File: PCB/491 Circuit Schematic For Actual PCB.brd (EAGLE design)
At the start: 160 x 100 mm, 27 parts

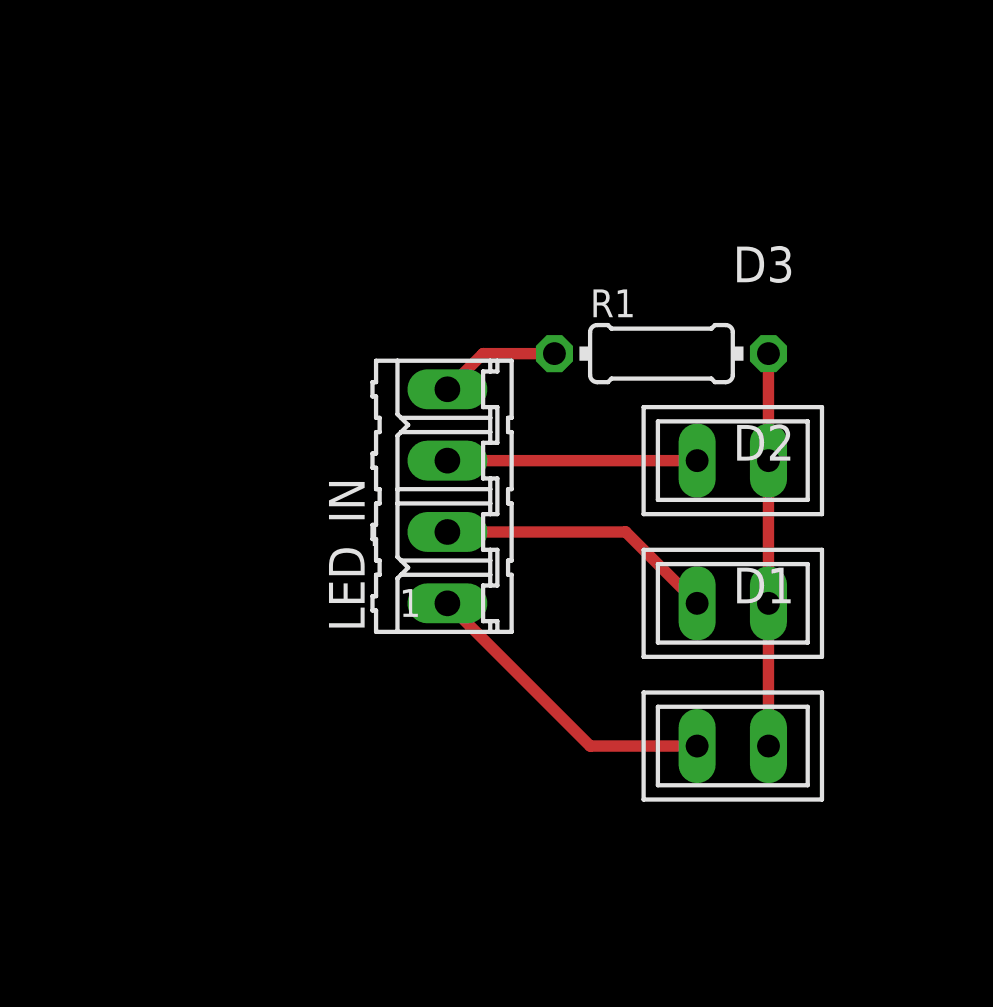
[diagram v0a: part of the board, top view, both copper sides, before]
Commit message: Added 5mm LEDs
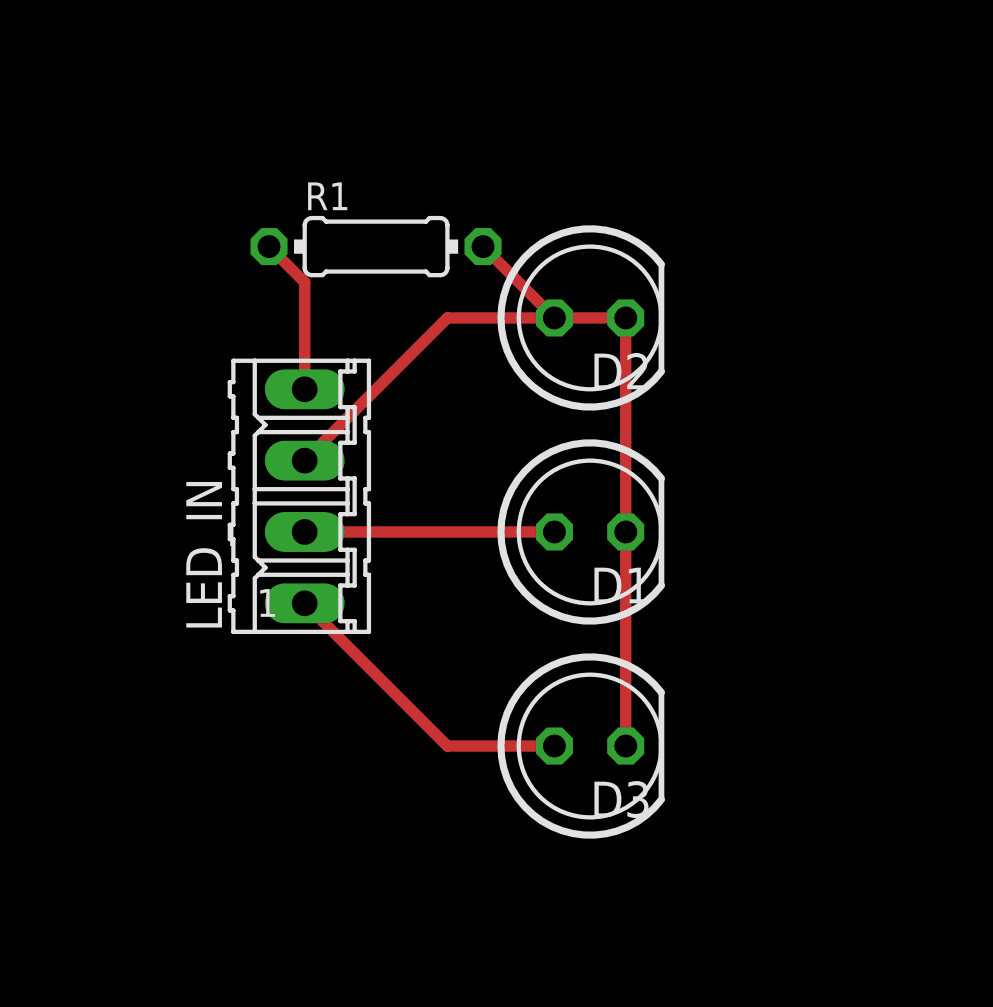
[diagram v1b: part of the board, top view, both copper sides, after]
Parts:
- D1, D2, D3: value U57X32 -> (none); device led:U57X32 -> led:LED5MM
- moved R1 10.9 mm to (135.9, 59.7)
- moved D3 7.18 mm to (143.5, 57.1)
- moved D2 5.68 mm to (143.5, 49.5)
- moved D1 5.08 mm to (143.5, 41.9)
- moved LED_IN 5.08 mm to (133.3, 50.8)
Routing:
- net N$10: track 14.0 -> 21.4 mm
- net N$1: track 8.89 -> 11.0 mm
- net N$30: track 4.34 -> 5.61 mm
- net N$3: track 9.94 -> 8.89 mm
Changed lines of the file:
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@@
 </autorouter>
 <elements>
-<element name="D1" library="led" library_urn="urn:adsk.eagle:library:259" package="U57X32" package3d_urn="urn:adsk.eagle:package:15789/1" value="U57X32" x="148.59" y="41.91" smashed="yes">
-<attribute name="NAME" x="148.59" y="46.99" size="1.27" layer="25" ratio="10"/>
-<attribute name="POPULARITY" value="0" x="148.59" y="41.91" size="1.778" layer="27" display="off"/>
-<attribute name="VALUE" x="148.59" y="44.45" size="1.27" layer="27" ratio="10"/>
-</element>
-<element name="D2" library="led" library_urn="urn:adsk.eagle:library:259" package="U57X32" package3d_urn="urn:adsk.eagle:package:15789/1" value="U57X32" x="148.59" y="46.99" smashed="yes">
-<attribute name="NAME" x="148.59" y="52.07" size="1.27" layer="25" ratio="10"/>
-<attribute name="POPULARITY" value="0" x="148.59" y="46.99" size="1.778" layer="27" display="off"/>
-<attribute name="VALUE" x="148.59" y="49.53" size="1.27" layer="27" ratio="10"/>
-</element>
-<element name="D3" library="led" library_urn="urn:adsk.eagle:library:259" package="U57X32" package3d_urn="urn:adsk.eagle:package:15789/1" value="U57X32" x="148.59" y="52.07" smashed="yes">
-<attribute name="NAME" x="148.59" y="58.42" size="1.27" layer="25" ratio="10"/>
-<attribute name="POPULARITY" value="0" x="148.59" y="52.07" size="1.778" layer="27" display="off"/>
-<attribute name="VALUE" x="148.59" y="55.88" size="1.27" layer="27" ratio="10"/>
+<element name="D1" library="led" library_urn="urn:adsk.eagle:library:259" package="LED5MM" package3d_urn="urn:adsk.eagle:package:15799/2" value="" x="143.51" y="41.91" smashed="yes">
+<attribute name="NAME" x="143.51" y="46.99" size="1.27" layer="25" ratio="10"/>
+<attribute name="POPULARITY" value="93" x="143.51" y="41.91" size="1.778" layer="27" display="off"/>
+<attribute name="VALUE" x="143.51" y="44.45" size="1.27" layer="27" ratio="10"/>
+</element>
+<element name="D2" library="led" library_urn="urn:adsk.eagle:library:259" package="LED5MM" package3d_urn="urn:adsk.eagle:package:15799/2" value="" x="143.51" y="49.53" smashed="yes">
+<attribute name="NAME" x="143.51" y="54.61" size="1.27" layer="25" ratio="10"/>
+<attribute name="POPULARITY" value="93" x="143.51" y="49.53" size="1.778" layer="27" display="off"/>
+<attribute name="VALUE" x="143.51" y="52.07" size="1.27" layer="27" ratio="10"/>
+</element>
+<element name="D3" library="led" library_urn="urn:adsk.eagle:library:259" package="LED5MM" package3d_urn="urn:adsk.eagle:package:15799/2" value="" x="143.51" y="57.15" smashed="yes">
+<attribute name="NAME" x="143.51" y="39.37" size="1.27" layer="25" ratio="10"/>
+<attribute name="POPULARITY" value="93" x="143.51" y="57.15" size="1.778" layer="27" display="off"/>
+<attribute name="VALUE" x="143.51" y="60.96" size="1.27" layer="27" ratio="10"/>
 </element>
 <element name="RELAY" library="SRD-05VDC-SL-C" package="RELAY_SRD-05VDC-SL-C" value="SRD-05VDC-SL-C" x="34.29" y="25.4" smashed="yes" rot="R270">
@@
 <element name="U$1" library="cool_safe_lib" package="FEATHER_ONLY" value="TEMPLATE_ARGON/BORON/XENONFEATHER_ONLY" x="86.36" y="77.47" smashed="yes" rot="R270"/>
 <element name="LOCK_SWITCH" library="cool_safe_lib" package="02P" value="LOCK_SWITCH02P" x="106.68" y="7.62" smashed="yes" rot="MR180"/>
-<element name="R1" library="rcl" library_urn="urn:adsk.eagle:library:334" package="0204/7" package3d_urn="urn:adsk.eagle:package:23498/2" value="" x="146.05" y="55.88" smashed="yes">
-<attribute name="NAME" x="143.51" y="57.1754" size="0.9906" layer="25" ratio="10"/>
-<attribute name="POPULARITY" value="48" x="146.05" y="55.88" size="1.778" layer="27" display="off"/>
-<attribute name="SPICEPREFIX" value="R" x="146.05" y="55.88" size="1.778" layer="27" display="off"/>
-<attribute name="VALUE" x="144.4244" y="55.3974" size="0.9906" layer="27" ratio="10"/>
+<element name="R1" library="rcl" library_urn="urn:adsk.eagle:library:334" package="0204/7" package3d_urn="urn:adsk.eagle:package:23498/2" value="" x="135.89" y="59.69" smashed="yes">
+<attribute name="NAME" x="133.35" y="60.9854" size="0.9906" layer="25" ratio="10"/>
+<attribute name="POPULARITY" value="48" x="135.89" y="59.69" size="1.778" layer="27" display="off"/>
+<attribute name="SPICEPREFIX" value="R" x="135.89" y="59.69" size="1.778" layer="27" display="off"/>
+<attribute name="VALUE" x="134.2644" y="59.2074" size="0.9906" layer="27" ratio="10"/>
 </element>
 <element name="R2" library="rcl" library_urn="urn:adsk.eagle:library:334" package="0204/7" package3d_urn="urn:adsk.eagle:package:23498/2" value="" x="96.52" y="7.62" smashed="yes">
@@
 <attribute name="VALUE" x="123.2154" y="48.514" size="1.27" layer="27" ratio="10" rot="R90"/>
 </element>
-<element name="LED_IN" library="con-amp-quick" library_urn="urn:adsk.eagle:library:125" package="04P" package3d_urn="urn:adsk.eagle:package:5958/1" value="" x="138.43" y="50.8" smashed="yes" rot="R90">
-<attribute name="MF" value="" x="138.43" y="50.8" size="1.778" layer="27" rot="R90" display="off"/>
-<attribute name="MPN" value="" x="138.43" y="50.8" size="1.778" layer="27" rot="R90" display="off"/>
-<attribute name="NAME" x="135.4836" y="45.974" size="1.27" layer="25" ratio="10" rot="R90"/>
-<attribute name="OC_FARNELL" value="unknown" x="138.43" y="50.8" size="1.778" layer="27" rot="R90" display="off"/>
-<attribute name="OC_NEWARK" value="unknown" x="138.43" y="50.8" size="1.778" layer="27" rot="R90" display="off"/>
-<attribute name="POPULARITY" value="19" x="138.43" y="50.8" size="1.778" layer="27" rot="R90" display="off"/>
-<attribute name="VALUE" x="142.2654" y="45.974" size="1.27" layer="27" ratio="10" rot="R90"/>
+<element name="LED_IN" library="con-amp-quick" library_urn="urn:adsk.eagle:library:125" package="04P" package3d_urn="urn:adsk.eagle:package:5958/1" value="" x="133.35" y="50.8" smashed="yes" rot="R90">
+<attribute name="MF" value="" x="133.35" y="50.8" size="1.778" layer="27" rot="R90" display="off"/>
+<attribute name="MPN" value="" x="133.35" y="50.8" size="1.778" layer="27" rot="R90" display="off"/>
+<attribute name="NAME" x="130.4036" y="45.974" size="1.27" layer="25" ratio="10" rot="R90"/>
+<attribute name="OC_FARNELL" value="unknown" x="133.35" y="50.8" size="1.778" layer="27" rot="R90" display="off"/>
+<attribute name="OC_NEWARK" value="unknown" x="133.35" y="50.8" size="1.778" layer="27" rot="R90" display="off"/>
+<attribute name="POPULARITY" value="19" x="133.35" y="50.8" size="1.778" layer="27" rot="R90" display="off"/>
+<attribute name="VALUE" x="137.1854" y="45.974" size="1.27" layer="27" ratio="10" rot="R90"/>
 </element>
 </elements>
@@
 <contactref element="R1" pad="2"/>
 <contactref element="D3" pad="K"/>
-<wire x1="149.86" y1="55.88" x2="149.86" y2="52.07" width="0.4064" layer="1"/>
-<wire x1="149.86" y1="52.07" x2="149.86" y2="46.99" width="0.4064" layer="1"/>
-<wire x1="149.86" y1="46.99" x2="149.86" y2="41.91" width="0.4064" layer="1"/>
+<wire x1="142.24" y1="57.15" x2="144.78" y2="57.15" width="0.4064" layer="1"/>
+<wire x1="142.24" y1="57.15" x2="139.7" y2="59.69" width="0.4064" layer="1"/>
+<wire x1="144.78" y1="57.15" x2="144.78" y2="49.53" width="0.4064" layer="1"/>
+<wire x1="144.78" y1="49.53" x2="144.78" y2="41.91" width="0.4064" layer="1"/>
 </signal>
 <signal name="N$7">
@@
 <contactref element="D3" pad="A"/>
 <contactref element="LED_IN" pad="3"/>
-<wire x1="138.43" y1="52.07" x2="147.32" y2="52.07" width="0.4064" layer="1"/>
+<wire x1="142.24" y1="57.15" x2="138.43" y2="57.15" width="0.4064" layer="1"/>
+<wire x1="133.35" y1="52.07" x2="138.43" y2="57.15" width="0.4064" layer="1"/>
 </signal>
 <signal name="N$3">
 <contactref element="LED_IN" pad="2"/>
 <contactref element="D2" pad="A"/>
-<wire x1="147.32" y1="46.99" x2="144.78" y2="49.53" width="0.4064" layer="1"/>
-<wire x1="144.78" y1="49.53" x2="138.43" y2="49.53" width="0.4064" layer="1"/>
+<wire x1="142.24" y1="49.53" x2="133.35" y2="49.53" width="0.4064" layer="1"/>
 </signal>
 <signal name="N$5">
 <contactref element="LED_IN" pad="1"/>
 <contactref element="D1" pad="A"/>
-<wire x1="138.43" y1="46.99" x2="143.51" y2="41.91" width="0.4064" layer="1"/>
-<wire x1="143.51" y1="41.91" x2="147.32" y2="41.91" width="0.4064" layer="1"/>
+<wire x1="133.35" y1="46.99" x2="138.43" y2="41.91" width="0.4064" layer="1"/>
+<wire x1="138.43" y1="41.91" x2="142.24" y2="41.91" width="0.4064" layer="1"/>
 </signal>
 <signal name="N$30">
 <contactref element="LED_IN" pad="4"/>
 <contactref element="R1" pad="1"/>
-<wire x1="138.43" y1="54.61" x2="139.7" y2="55.88" width="0.4064" layer="1"/>
-<wire x1="139.7" y1="55.88" x2="142.24" y2="55.88" width="0.4064" layer="1"/>
+<wire x1="132.08" y1="59.69" x2="133.35" y2="58.42" width="0.4064" layer="1"/>
+<wire x1="133.35" y1="58.42" x2="133.35" y2="54.61" width="0.4064" layer="1"/>
 </signal>
 </signals>

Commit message: Update to PCB
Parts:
- removed 12V_IN, BATTERY: 12V, con-amp-quick:02P
- removed D1, D2, D3: (no value), led:LED5MM
- removed L2: SOLENOID, rcl:0207/5V
- removed LED_IN, LED_OUT: (no value), con-amp-quick:04P
- removed R1: (no value), rcl:0204/7
- added JP1: (no value), pinhead:1X04/90
- added SOLENOID: (no value), SparkFun-Connectors:JST-2-SMD
- added X1, X2: 1751248, con-phoenix-350:1751248
- LOCK_SWITCH: value LOCK_SWITCH02P -> LOCK_SWITCHSCREW_TERMINAL; device cool_safe_lib:02P -> cool_safe_lib:1751248
- R2: device rcl:0204/7 -> rcl:0207/10
- RELAY: value SRD-05VDC-SL-C -> ZF112; device SRD-05VDC-SL-C:RELAY_SRD-05VDC-SL-C -> relay:ZF112
- U$3: value FPS -> FPSQWIIC; device cool_safe_lib:JST -> cool_safe_lib:1X04_1MM_RA
- moved D5 70.2 mm to (8.89, 18.0), turned to 270 degrees
- moved C1 50.3 mm to (7.62, 40.9), turned to 180 degrees
- moved D6 50.1 mm to (14.0, 26.9), turned to 0 degrees
- moved C2 47.6 mm to (7.62, 49.8), turned to 180 degrees
- moved R4 45.6 mm to (14.0, 33.3), turned to 180 degrees
- moved R2 34.9 mm to (85.1, 40.6), turned to 270 degrees
- moved U$2 33.3 mm to (35.6, 67.3)
- moved U$1 33.0 mm to (54.6, 68.6)
- moved SP1 30.6 mm to (17.8, 50.8), turned to 0 degrees
- moved U$3 29.6 mm to (86.4, 12.7), turned to 90 degrees
- moved LOCK_SWITCH 26.9 mm to (87.6, 26.7), turned to 270 degrees
- moved T2 12.6 mm to (27.9, 50.8)
- moved T1 10.9 mm to (27.9, 40.6)
- moved R3 10.9 mm to (36.8, 40.6)
- moved R5 10.2 mm to (36.8, 50.8)
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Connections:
- removed net N$10: D1.K, D2.K, D3.K, R1.2
- removed net N$14: BATTERY.1, D6.A, R4.1
- removed net N$19: U$1.18B, U$1.18T
- removed net N$22: U$1.19B, U$1.19T
- removed net N$25: U$1.20B, U$1.20T
- removed net N$3: D2.A, LED_IN.2
- removed net N$30: LED_IN.4, R1.1
- removed net N$5: D1.A, LED_IN.1
- net +12V: now also RELAY.P, U$2.IN+.2; no longer RELAY.COM
- net +3V3: now also LOCK_SWITCH.2, RELAY.1, U$1.P$14, U$2.OUT+.2; no longer LOCK_SWITCH.1, RELAY.A1
- net 0: now also JP1.1, SOLENOID.2, U$1.P$16, X1.1, X2.1; no longer 12V_IN.2, BATTERY.2, L2.2, LED_OUT.4
- net N$1: now also D6.A, R4.1, X2.2; no longer D3.A, LED_IN.3
- net N$11: now also RELAY.2; no longer RELAY.A2
- net N$13: now also RELAY.S, SOLENOID.1; no longer L2.1, RELAY.NO
- net N$16: now also U$1.P$26
- net N$18: now also U$1.P$21
- net N$28: now also U$1.P$27
- net N$29: now also X1.2; no longer 12V_IN.1
- net N$4: now also U$1.P$17
- net N$6: now also JP1.4, U$1.P$6; no longer LED_OUT.1
- net N$7: now also JP1.3, U$1.P$5; no longer LED_OUT.2
- net N$8: now also JP1.2, U$1.P$4; no longer LED_OUT.3
- net N$9: now also LOCK_SWITCH.1, U$1.P$7; no longer LOCK_SWITCH.2
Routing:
- net N$9: track 58.8 -> 14.6 mm
- net N$18: track 54.2 -> 17.8 mm
- net N$31: track 7.74 -> 43.6 mm
- net N$4: track 53.0 -> 17.8 mm
- net N$14: track 22.9 -> 0.00 mm
- net N$10: track 21.4 -> 0.00 mm
- net N$1: track 11.0 -> 27.4 mm
- net +3V3: track 164.9 -> 179.7 mm
- net N$28: track 57.6 -> 46.4 mm
- net N$5: track 11.0 -> 0.00 mm
- net N$3: track 8.89 -> 0.00 mm
- net N$30: track 5.61 -> 0.00 mm
- net +12V: track 103.3 -> 98.1 mm
- net N$13: track 15.2 -> 10.1 mm
- net 0: track 386.1 -> 390.2 mm
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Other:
- board size 160 x 100 mm -> 95.2 x 77.5 mm
- board text added: "12V"
- board text added: "BATT"
- board text added: "LED"
- board text added: "LOCK"
- board text added: "SCANNER"
